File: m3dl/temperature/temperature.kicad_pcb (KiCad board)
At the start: 2 copper layers, 40 x 33 mm, 44 parts, among them IC1 LTC2983, J1 WEST TOP, J2 EAST TOP, J3 WEST BOT, J4 EAST BOT, J5 SOUTH TOP, J6 SOUTH BOT, J7 TEMP1, J8 TEMP9, J9 TEMP2-8

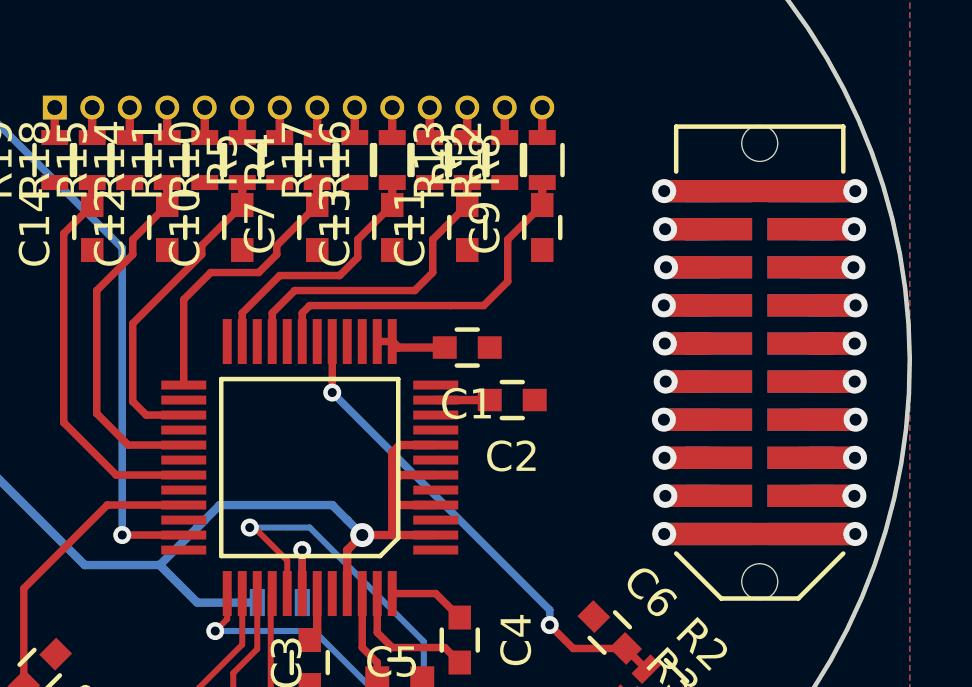
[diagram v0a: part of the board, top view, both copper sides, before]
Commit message: Tidyied up Main & Checked Connector Clearance for Sensors
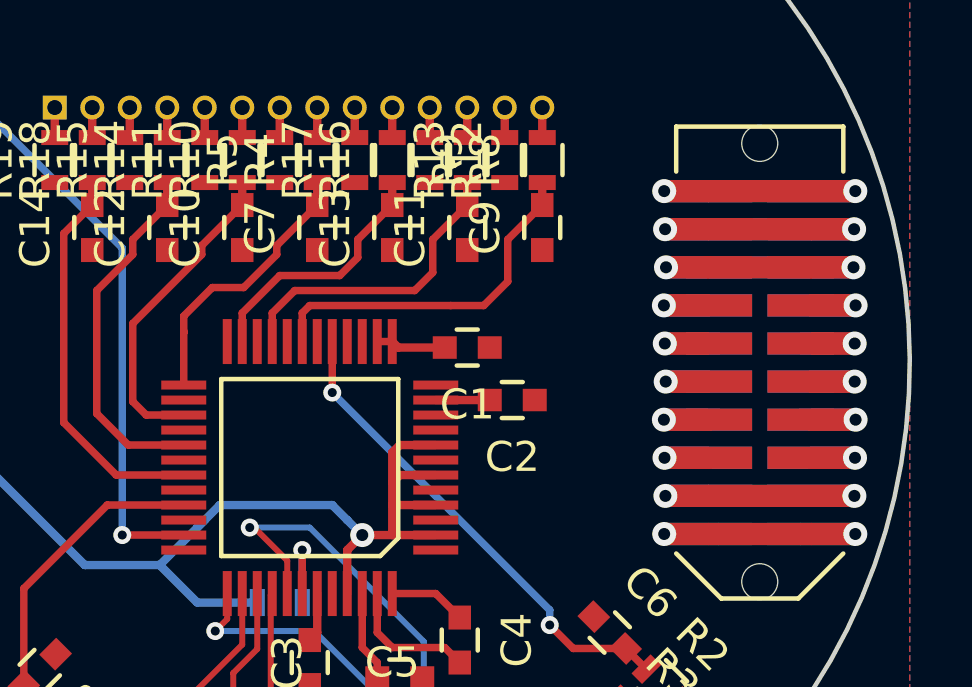
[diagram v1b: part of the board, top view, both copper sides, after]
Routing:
- net /PYRO_SO: track 6.44 -> 12.6 mm
- net /PYRO_SI: track 6.34 -> 12.5 mm
- net /CHARGE: track 6.44 -> 12.6 mm
- net GND: track 73.5 -> 76.2 mm
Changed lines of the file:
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@@
   (general
     (links 171)
-    (no_connects 3)
+    (no_connects 0)
     (area 79.923999 86.924999 120.076001 120.076001)
     (thickness 1.6)
     (drawings 5)
-    (tracks 369)
+    (tracks 378)
     (zones 0)
     (modules 44)
@@
     (35 F.Paste user hide)
     (36 B.SilkS user hide)
-    (37 F.SilkS user)
+    (37 F.SilkS user hide)
     (38 B.Mask user hide)
     (39 F.Mask user hide)
-    (40 Dwgs.User user)
+    (40 Dwgs.User user hide)
     (41 Cmts.User user hide)
     (42 Eco1.User user hide)
     (43 Eco2.User user hide)
     (44 Edge.Cuts user)
-    (45 Margin user)
+    (45 Margin user hide)
     (46 B.CrtYd user hide)
     (47 F.CrtYd user hide)
@@
   )
   (setup
-    (last_trace_width 0.28)
+    (last_trace_width 0.74)
     (user_trace_width 0.2)
     (user_trace_width 0.28)
@@
   (gr_line (start 100 87) (end 82 87) (layer Dwgs.User) (width 0.2))
   (gr_circle (center 100 100) (end 120 100) (layer Dwgs.User) (width 0.2))
+  (segment (start 113.635 94.285) (end 116.365 94.285) (width 0.74) (layer B.Cu) (net 1))
   (segment (start 83.635 94.285) (end 81.815 94.285) (width 0.74) (layer B.Cu) (net 1))
   (segment (start 86.365 94.285) (end 83.635 94.285) (width 0.74) (layer B.Cu) (net 1))
@@
   (segment (start 97.75 99.3) (end 97.75 98.35) (width 0.25) (layer F.Cu) (net 9))
   (segment (start 102.75 94) (end 102.75 94.75) (width 0.28) (layer F.Cu) (net 9))
+  (segment (start 95.8 99) (end 95.8 98.45) (width 0.25) (layer F.Cu) (net 10))
+  (segment (start 95.8 98.45) (end 96.75 97.5) (width 0.25) (layer F.Cu) (net 10))
+  (segment (start 96.75 97.5) (end 97.8 97.5) (width 0.25) (layer F.Cu) (net 10))
+  (segment (start 97.8 97.5) (end 98.9 96.4) (width 0.25) (layer F.Cu) (net 10))
   (segment (start 98.9 96.4) (end 98.9 96.1) (width 0.25) (layer F.Cu) (net 10))
   (segment (start 98.9 96.1) (end 100.25 94.75) (width 0.25) (layer F.Cu) (net 10))
-  (segment (start 98.3 97) (end 98.9 96.4) (width 0.25) (layer F.Cu) (net 10))
-  (segment (start 96.7 97) (end 98.3 97) (width 0.25) (layer F.Cu) (net 10))
-  (segment (start 95.8 97.9) (end 96.7 97) (width 0.25) (layer F.Cu) (net 10))
-  (segment (start 95.8 100.75) (end 95.8 97.9) (width 0.25) (layer F.Cu) (net 10))
+  (segment (start 95.8 100.75) (end 95.8 99) (width 0.25) (layer F.Cu) (net 10))
+  (segment (start 95.8 99) (end 95.8 98.95) (width 0.25) (layer F.Cu) (net 10))
   (segment (start 100.25 94) (end 100.25 94.75) (width 0.28) (layer F.Cu) (net 10))
   (segment (start 96.4 96.4) (end 96.4 96.1) (width 0.25) (layer F.Cu) (net 11))
@@
   (via (at 88.155 104.445) (size 0.8) (drill 0.4) (layers F.Cu B.Cu) (net 41))
   (segment (start 86.715 104.445) (end 88.155 104.445) (width 0.74) (layer F.Cu) (net 41))
+  (segment (start 116.365 95.555) (end 113.635 95.555) (width 0.74) (layer B.Cu) (net 42))
+  (segment (start 113.285 95.555) (end 116.715 95.555) (width 0.74) (layer F.Cu) (net 42))
   (segment (start 116.365 95.555) (end 118.145 95.555) (width 0.74) (layer B.Cu) (net 42))
   (segment (start 111.845 95.555) (end 113.635 95.555) (width 0.74) (layer B.Cu) (net 42))
@@
   (via (at 111.845 95.555) (size 0.8) (drill 0.4) (layers F.Cu B.Cu) (net 42))
   (segment (start 113.285 95.555) (end 111.845 95.555) (width 0.74) (layer F.Cu) (net 42))
+  (segment (start 113.635 96.825) (end 116.365 96.825) (width 0.74) (layer B.Cu) (net 43))
+  (segment (start 113.285 96.825) (end 116.715 96.825) (width 0.74) (layer F.Cu) (net 43))
   (segment (start 118.125 96.825) (end 116.365 96.825) (width 0.74) (layer B.Cu) (net 43))
   (segment (start 113.635 96.825) (end 111.875 96.825) (width 0.74) (layer B.Cu) (net 43))
@@
   (via (at 118.175 103.175) (size 0.8) (drill 0.4) (layers F.Cu B.Cu) (net 53))
   (segment (start 116.715 103.175) (end 118.175 103.175) (width 0.74) (layer F.Cu) (net 53))
+  (segment (start 116.365 104.445) (end 113.635 104.445) (width 0.74) (layer B.Cu) (net 54))
+  (segment (start 113.285 104.445) (end 116.715 104.445) (width 0.74) (layer F.Cu) (net 54))
   (segment (start 117.455 104.445) (end 118.155 104.445) (width 0.74) (layer B.Cu) (net 54))
   (segment (start 116.365 104.445) (end 117.455 104.445) (width 0.74) (layer B.Cu) (net 54))

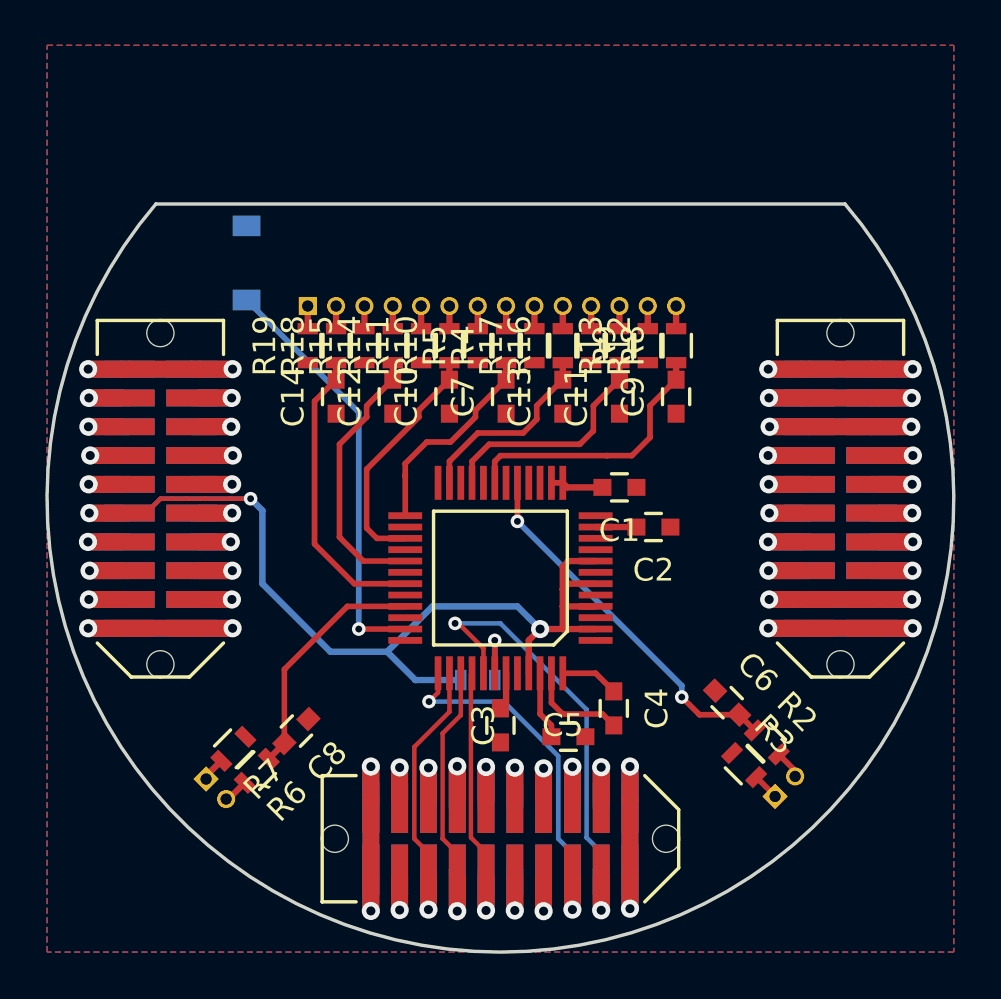
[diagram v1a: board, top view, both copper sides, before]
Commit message: Completed all of Pressure Strain and Temperature
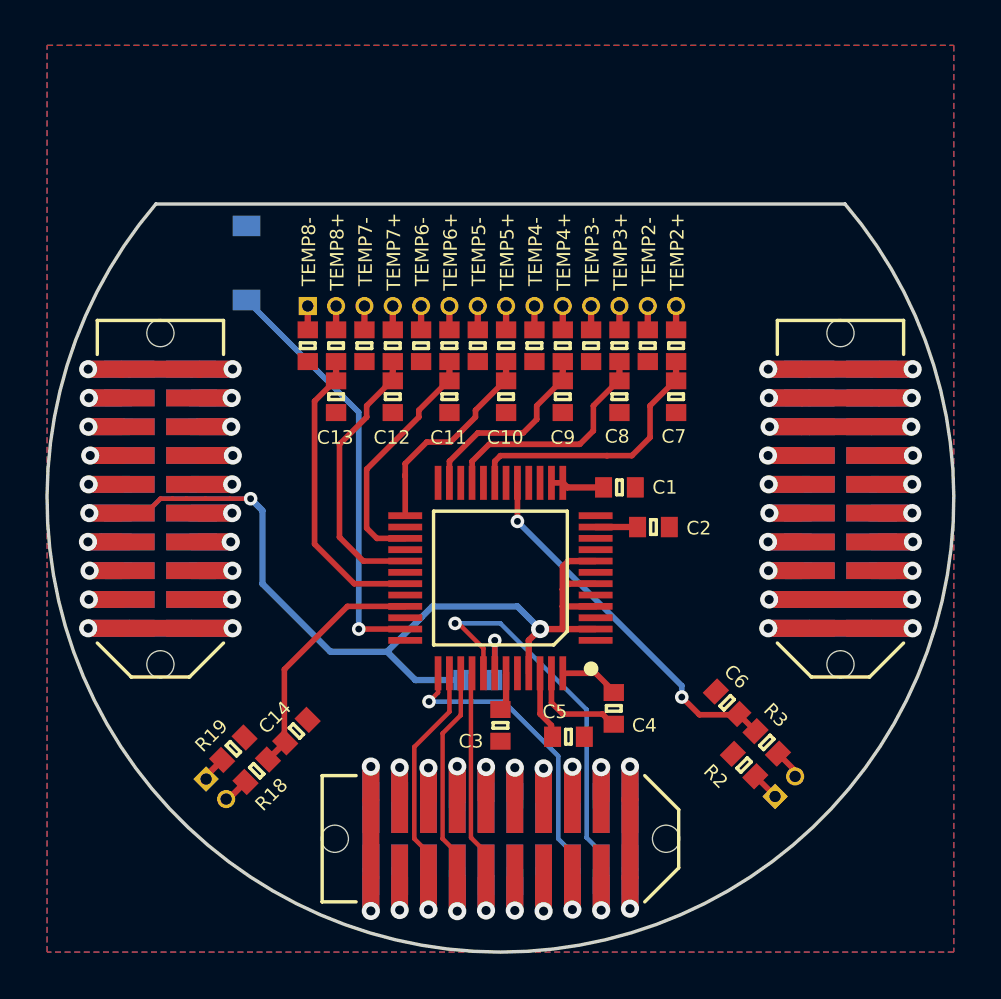
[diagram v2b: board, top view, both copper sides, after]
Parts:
- C1, C10, C11, C12, C13, C14, C2, C3, C4, C5, C6, C7, C8, C9: footprint Capacitors_SMD:C_0603 -> agg:0603-L
- R1, R10, R11, R12, R13, R14, R15, R16, R17, R18, R19, R2, R3, R4, R5, R6, R7, R8, R9: footprint Resistors_SMD:R_0603 -> agg:0603-L
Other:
- board text added: "C1"
- board text added: "C10"
- board text added: "C11"
- board text added: "C12"
- board text added: "C13"
- board text added: "C14"
- board text added: "C2"
- board text added: "C3"
- board text added: "C4"
- board text added: "C5"
- board text added: "C6"
- board text added: "C7"
- board text added: "C8"
- board text added: "C9"
- board text added: "D1"
- board text added: "R1"
- board text added: "R18"
- board text added: "R19"
- board text added: "R2"
- board text added: "R3"
- board text added: "TEMP1+"
- board text added: "TEMP1-"
- board text added: "TEMP2+"
- board text added: "TEMP2-"
- board text added: "TEMP3+"
- board text added: "TEMP3-"
- board text added: "TEMP4+"
- board text added: "TEMP4-"
- board text added: "TEMP5+"
- board text added: "TEMP5-"
- board text added: "TEMP6+"
- board text added: "TEMP6-"
- board text added: "TEMP7+"
- board text added: "TEMP7-"
- board text added: "TEMP8+"
- board text added: "TEMP8-"
- board text added: "TEMP9+"
- board text added: "TEMP9-"

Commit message: Almost ready to generate gerbers
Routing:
- net /SPI1_MOSI: track 12.6 -> 13.7 mm
- net /SPI1_MISO: track 12.9 -> 14.0 mm
- net /SPI1_CS: track 20.7 -> 21.5 mm
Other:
- net class Default: clearance 0.1 -> 0.127
- rule pad_to_mask_clearance: 0.2 -> 0
- rule trace_clearance: 0.1 -> 0.127
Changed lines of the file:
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@@
     (thickness 1.6)
     (drawings 60)
-    (tracks 378)
+    (tracks 385)
     (zones 0)
     (modules 44)
@@
     (user_trace_width 0.28)
     (user_trace_width 0.74)
-    (trace_clearance 0.1)
+    (trace_clearance 0.127)
     (zone_clearance 0.15)
     (zone_45_only no)
@@
     (pad_size 1.524 1.524)
     (pad_drill 0.762)
-    (pad_to_mask_clearance 0.2)
+    (pad_to_mask_clearance 0)
     (aux_axis_origin 0 0)
     (visible_elements FFFFFE1F)
@@
   (net 83 /TEMP9-)
   (net_class Default "This is the default net class."
-    (clearance 0.1)
+    (clearance 0.127)
     (trace_width 0.25)
     (via_dia 0.6)
@@
     (effects (font (size 0.6 0.6) (thickness 0.12)))
   )
-  (gr_text C1 (at 107.25 99.5 360) (layer F.SilkS)
+  (gr_text C1 (at 107.25 99.5) (layer F.SilkS)
     (effects (font (size 0.6 0.6) (thickness 0.12)))
   )
@@
   (segment (start 93.75 96.185) (end 93.75 105.75) (width 0.25) (layer B.Cu) (net 16))
   (segment (start 88.8 91.235) (end 93.75 96.185) (width 0.25) (layer B.Cu) (net 16))
+  (segment (start 103.175 116.365) (end 103.175 115.625) (width 0.2) (layer B.Cu) (net 17))
+  (segment (start 103.175 115.625) (end 102.547999 114.997999) (width 0.2) (layer B.Cu) (net 17))
+  (segment (start 102.547999 114.997999) (end 102.547999 111.352001) (width 0.2) (layer B.Cu) (net 17))
+  (segment (start 102.547999 111.352001) (end 102.55 111.35) (width 0.2) (layer B.Cu) (net 17))
   (segment (start 96.85 108.95) (end 100.15 108.95) (width 0.2) (layer B.Cu) (net 17))
   (segment (start 100.15 108.95) (end 102.55 111.35) (width 0.2) (layer B.Cu) (net 17))
@@
   (segment (start 97.25 108.55) (end 96.85 108.95) (width 0.2) (layer F.Cu) (net 17))
   (segment (start 97.25 107.7) (end 97.25 108.55) (width 0.2) (layer F.Cu) (net 17))
-  (segment (start 102.55 115) (end 102.55 111.35) (width 0.2) (layer B.Cu) (net 17))
-  (segment (start 103.175 115.625) (end 102.55 115) (width 0.2) (layer B.Cu) (net 17))
-  (segment (start 103.175 116.365) (end 103.175 115.625) (width 0.2) (layer B.Cu) (net 17))
   (segment (start 103.175 116.365) (end 103.175 118.125) (width 0.74) (layer B.Cu) (net 17))
   (via (at 103.175 118.125) (size 0.8) (drill 0.4) (layers F.Cu B.Cu) (net 17))
   (segment (start 103.175 116.715) (end 103.175 118.125) (width 0.74) (layer F.Cu) (net 17))
-  (segment (start 96.2 115) (end 96.825 115.625) (width 0.2) (layer F.Cu) (net 18))
-  (segment (start 96.825 115.625) (end 96.825 116.715) (width 0.2) (layer F.Cu) (net 18))
-  (segment (start 96.2 110.95) (end 96.2 115) (width 0.2) (layer F.Cu) (net 18))
-  (segment (start 97.75 109.4) (end 96.2 110.95) (width 0.2) (layer F.Cu) (net 18))
-  (segment (start 97.75 107.7) (end 97.75 109.4) (width 0.2) (layer F.Cu) (net 18))
+  (segment (start 96.825 116.715) (end 96.825 115.625) (width 0.2) (layer F.Cu) (net 18))
+  (segment (start 96.825 115.625) (end 96.197999 114.997999) (width 0.2) (layer F.Cu) (net 18))
+  (segment (start 96.197999 114.997999) (end 96.197999 110.952001) (width 0.2) (layer F.Cu) (net 18))
+  (segment (start 96.197999 110.952001) (end 97.75 109.4) (width 0.2) (layer F.Cu) (net 18))
+  (segment (start 97.75 109.4) (end 97.75 107.7) (width 0.2) (layer F.Cu) (net 18))
   (segment (start 96.825 116.365) (end 96.825 118.125) (width 0.74) (layer B.Cu) (net 18))
   (via (at 96.825 118.125) (size 0.8) (drill 0.4) (layers F.Cu B.Cu) (net 18))
   (segment (start 96.825 116.715) (end 96.825 118.125) (width 0.74) (layer F.Cu) (net 18))
-  (segment (start 98.25 107.7) (end 98.25 109.55) (width 0.2) (layer F.Cu) (net 19))
-  (segment (start 98.25 109.55) (end 97.45 110.35) (width 0.2) (layer F.Cu) (net 19))
-  (segment (start 97.45 110.35) (end 97.45 115) (width 0.2) (layer F.Cu) (net 19))
-  (segment (start 97.45 115) (end 98.095 115.645) (width 0.2) (layer F.Cu) (net 19))
+  (segment (start 98.095 116.715) (end 98.095 115.625) (width 0.2) (layer F.Cu) (net 19))
+  (segment (start 98.095 115.625) (end 97.467999 114.997999) (width 0.2) (layer F.Cu) (net 19))
+  (segment (start 97.467999 110.332001) (end 98.25 109.55) (width 0.2) (layer F.Cu) (net 19))
+  (segment (start 97.467999 114.997999) (end 97.467999 110.332001) (width 0.2) (layer F.Cu) (net 19))
+  (segment (start 98.25 109.55) (end 98.25 107.7) (width 0.2) (layer F.Cu) (net 19))
   (segment (start 98.095 115.645) (end 98.095 116.715) (width 0.2) (layer F.Cu) (net 19))
   (segment (start 98.095 116.365) (end 98.095 118.195) (width 0.74) (layer B.Cu) (net 19))
   (via (at 98.095 118.195) (size 0.8) (drill 0.4) (layers F.Cu B.Cu) (net 19))
   (segment (start 98.095 116.715) (end 98.095 118.195) (width 0.74) (layer F.Cu) (net 19))
+  (segment (start 99.365 116.715) (end 99.365 115.523602) (width 0.2) (layer F.Cu) (net 20))
+  (segment (start 98.737999 114.896601) (end 98.737999 107.712001) (width 0.2) (layer F.Cu) (net 20))
+  (segment (start 99.365 115.523602) (end 98.737999 114.896601) (width 0.2) (layer F.Cu) (net 20))
+  (segment (start 98.737999 107.712001) (end 98.75 107.7) (width 0.2) (layer F.Cu) (net 20))
   (segment (start 99.365 116.715) (end 99.365 115.615) (width 0.2) (layer F.Cu) (net 20))
-  (segment (start 99.365 115.615) (end 98.7 114.95) (width 0.2) (layer F.Cu) (net 20))
-  (segment (start 98.7 114.95) (end 98.7 107.75) (width 0.2) (layer F.Cu) (net 20))
   (segment (start 98.7 107.75) (end 98.75 107.7) (width 0.2) (layer F.Cu) (net 20))
   (segment (start 99.365 116.365) (end 99.365 118.165) (width 0.74) (layer B.Cu) (net 20))
   (via (at 99.365 118.165) (size 0.8) (drill 0.4) (layers F.Cu B.Cu) (net 20))
   (segment (start 99.365 116.715) (end 99.365 118.165) (width 0.74) (layer F.Cu) (net 20))
+  (segment (start 103.802001 111.102001) (end 103.8 111.1) (width 0.2) (layer B.Cu) (net 21))
+  (segment (start 103.8 111.1) (end 103.8 109.3) (width 0.2) (layer B.Cu) (net 21))
+  (segment (start 104.445 116.365) (end 104.445 115.625) (width 0.2) (layer B.Cu) (net 21))
+  (segment (start 104.445 115.625) (end 103.802001 114.982001) (width 0.2) (layer B.Cu) (net 21))
+  (segment (start 103.802001 114.982001) (end 103.802001 111.102001) (width 0.2) (layer B.Cu) (net 21))
   (segment (start 98 105.5) (end 98.15 105.5) (width 0.2) (layer F.Cu) (net 21))
   (segment (start 98.15 105.5) (end 99.25 106.6) (width 0.2) (layer F.Cu) (net 21))
@@
   (segment (start 98 105.5) (end 100 105.5) (width 0.2) (layer B.Cu) (net 21))
   (segment (start 100 105.5) (end 103.8 109.3) (width 0.2) (layer B.Cu) (net 21))
-  (segment (start 103.8 114.95) (end 104.445 115.595) (width 0.2) (layer B.Cu) (net 21))
-  (segment (start 103.8 109.3) (end 103.8 114.95) (width 0.2) (layer B.Cu) (net 21))
   (segment (start 104.445 115.595) (end 104.445 116.365) (width 0.2) (layer B.Cu) (net 21))
   (via (at 98 105.5) (size 0.6) (drill 0.3) (layers F.Cu B.Cu) (net 21))

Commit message: All finished except logos
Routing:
- net GND: track 76.2 -> 188.3 mm, vias 12 -> 54

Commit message: All PCBs Finished
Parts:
- added G***: LOGO, logos:cusf_logo_full, B.Cu at (105.0, 101.5)
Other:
- board text added: "m3dl - Temp Matt Coates 11/03/16"

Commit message: Uploaded Gerbers
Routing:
- net GND: track 188.3 -> 198.5 mm, vias 54 -> 63
- net (no net): track 0.00 -> 7.24 mm, vias 0 -> 5
- net /CH1+: track 16.3 -> 18.1 mm
- net Net-(D1-Pad2): track 18.6 -> 19.3 mm
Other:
- board text added: "m3dl - Temp r1 Matt Coates 11/03/16"
- board text removed: "m3dl - Temp Matt Coates 11/03/16"

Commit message: Modifications as per review document
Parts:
- removed G***: LOGO, logos:cusf_logo_full
- added C15: 100n, agg:0603, B.Cu at (101.3, 106.7)
- C2: value 0.1u -> 100n
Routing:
- net GND: track 198.5 -> 215.5 mm, vias 63 -> 74
- net (no net): track 7.24 -> 0.00 mm, vias 5 -> 0
- net 3v3: track 54.2 -> 50.6 mm
- net /SPI1_MOSI: track 13.7 -> 12.6 mm
- net Net-(C4-Pad1): track 2.58 -> 3.44 mm
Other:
- net class Default: clearance 0.127 -> 0.15; trace_width 0.25 -> 0.2
- rule trace_clearance: 0.127 -> 0.15
- rule via_min_size: 0.4 -> 0.6
- board text added: "C15"

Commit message: Generated gerbers
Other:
- board text added: "m3dl - Temp r1 Matt Coates 12/06/16"
- board text removed: "m3dl - Temp r1 Matt Coates 11/03/16"
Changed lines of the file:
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@@
     (links 173)
     (no_connects 0)
-    (area 79.923999 86.924999 120.076001 120.076001)
+    (area 79.8 79.899999 120.100001 120.100001)
     (thickness 1.6)
     (drawings 62)
@@
     (effects (font (size 0.6 0.6) (thickness 0.12)) (justify mirror))
   )
-  (gr_text "m3dl - Temp r1\nMatt Coates\n11/03/16" (at 110.4 103.5) (layer B.SilkS)
+  (gr_text "m3dl - Temp r1\nMatt Coates\n12/06/16" (at 110.4 103.5) (layer B.SilkS)
     (effects (font (size 0.7 0.7) (thickness 0.1)) (justify left mirror))
   )
